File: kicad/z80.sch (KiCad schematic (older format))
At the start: 26 parts, among them J3 Conn_02x20_Odd_Even, J5 USB_B, J6 PWR, SW1 KS01Q, U1 Z80CPU, U2 74AHC14, U20 MIC5504-3.3YM5, U3 SST39SF010, U4 74AHC32, U5 AS6C1008-55PCN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

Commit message: Update to Kicad 5
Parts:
- C1, C2, C26, C3, C30, C4, C5, C6, C7: symbol C -> Device:C
- C24: symbol CP1_Small -> Device:CP1_Small
- D1: symbol LED_Small_ALT -> Device:LED_Small_ALT
- J3: symbol Conn_02x20_Odd_Even -> Connector_Generic:Conn_02x20_Odd_Even
- J5: symbol USB_B -> Connector:USB_B
- J6: symbol Conn_01x02 -> Connector_Generic:Conn_01x02
- R1, R18, R29: symbol R -> Device:R
- SW1: symbol SW_Push -> Switch:SW_Push
- U1: symbol Z80CPU -> CPU:Z80CPU
- U2: symbol 74HC14 -> 74xx:74HC14
- U20: symbol MIC5504-3.3YM5 -> Regulator_Linear:MIC5504-3.3YM5
- U3: symbol SST39SF010 -> Memory_Flash:SST39SF010
- U4: symbol 74LS32 -> 74xx:74LS32
- U5: symbol AS6C1008-55SIN -> headquarters:AS6C1008-55SIN
- U6: symbol 74LS138 -> 74xx:74LS138
- X1: symbol CXO_DIP8 -> Oscillator:CXO_DIP8
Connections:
- wire segments 237 -> 264

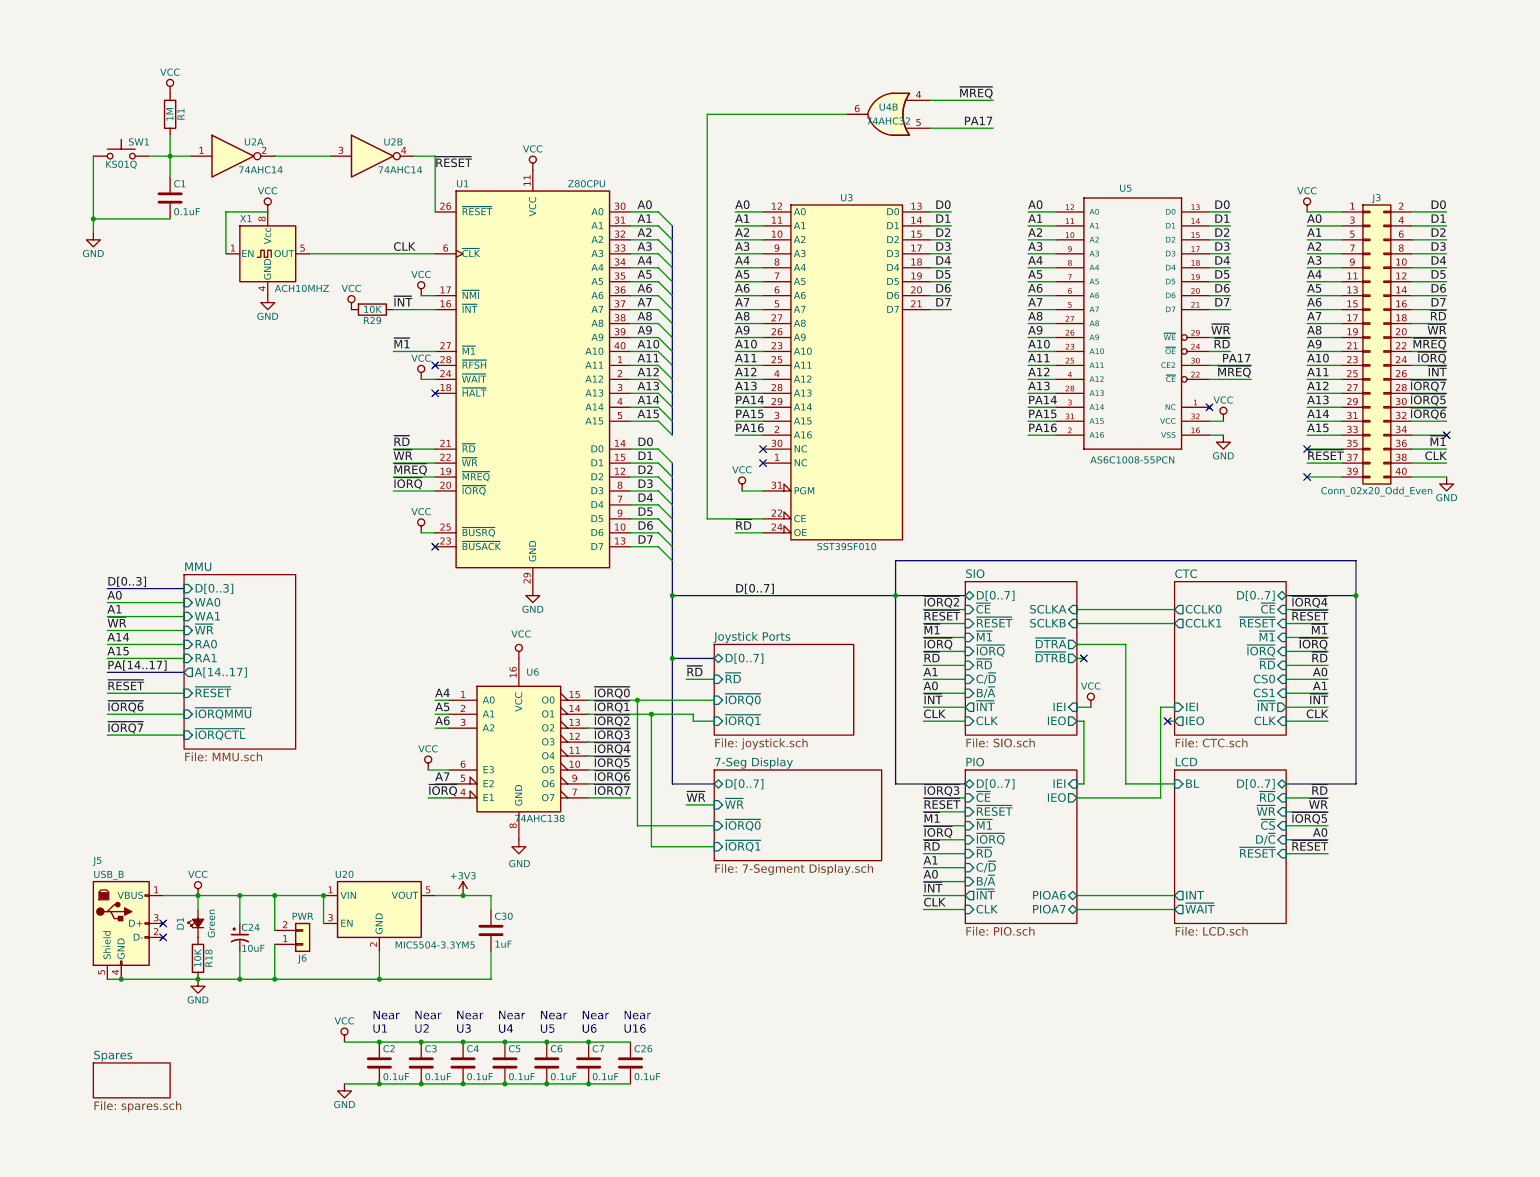
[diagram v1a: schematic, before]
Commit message: Working on SD card interface, cleaning up.
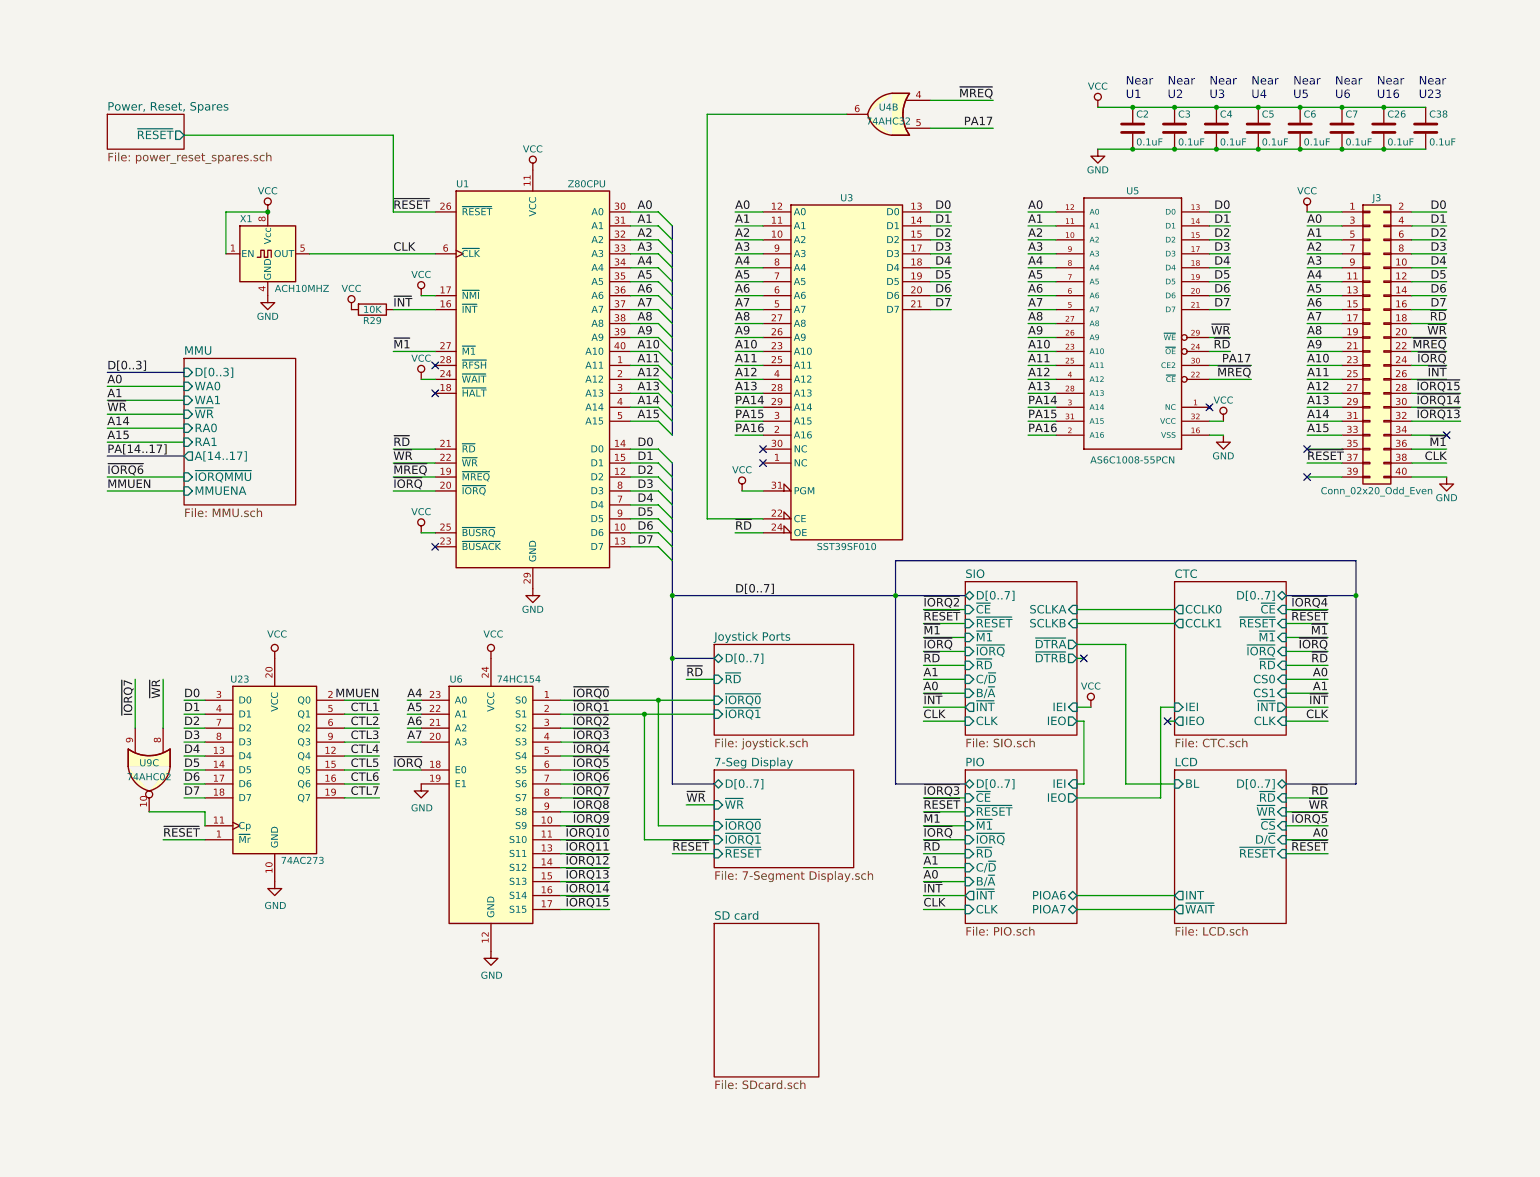
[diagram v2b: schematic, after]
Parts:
- removed C1: 0.1uF, Capacitors_THT:C_Disc_D4.3mm_W1.9mm_P5.00mm, symbol Device:C
- removed C24: 10uF, Capacitors_THT:CP_Radial_D5.0mm_P2.50mm, symbol Device:CP1_Small
- removed C30: 1uF, symbol Device:C
- removed D1: Green, LEDs:LED_D5.0mm, symbol Device:LED_Small_ALT
- removed J5: USB_B, z80_footprints:USB_B_E8144-B02022-L, symbol Connector:USB_B
- removed J6: PWR, Pin_Headers:Pin_Header_Straight_2x01_Pitch2.54mm, symbol Connector_Generic:Conn_01x02
- removed R1: 1M, Resistors_THT:R_Axial_DIN0204_L3.6mm_D1.6mm_P5.08mm_Horizontal, symbol Device:R
- removed R18: 10K, Resistors_THT:R_Axial_DIN0204_L3.6mm_D1.6mm_P5.08mm_Horizontal, symbol Device:R
- removed SW1: KS01Q, z80_footprints:KS-01Q-02, symbol Switch:SW_Push
- removed U2: 74AHC14, Housings_DIP:DIP-14_W7.62mm_LongPads, symbol 74xx:74HC14
- removed U20: MIC5504-3.3YM5, TO_SOT_Packages_SMD:SOT-23-5, symbol Regulator_Linear:MIC5504-3.3YM5
- removed U6: 74AHC138, Housings_DIP:DIP-16_W7.62mm_LongPads, symbol 74xx:74LS138
- added C38: 0.1uF, Capacitors_THT:C_Disc_D4.3mm_W1.9mm_P5.00mm, symbol Device:C
- added U23: 74AC273, symbol 74xx:74LS273
- added U6: 74HC154, symbol 74xx:74LS154
- added U9: 74AHC02, Housings_DIP:DIP-14_W7.62mm_LongPads, symbol 74xx:74HC02
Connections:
- net A4: now also U6.23 (A0)
- net A5: now also U6.22 (A1)
- net A6: now also U6.21 (A2)
- net A7: now also U6.20 (A3)
- net D0: now also U23.3 (D0)
- net D1: now also U23.4 (D1)
- net D2: now also U23.7 (D2)
- net D3: now also U23.8 (D3)
- net D4: now also U23.13 (D4)
- net D5: now also U23.14 (D5)
- net D6: now also U23.17 (D6)
- net D7: now also U23.18 (D7)
- net GND: now also C38.2, U23.10 (GND), U6.12 (GND), U6.19 (E1)
- net VCC: now also C38.1, U23.20 (VCC), U6.24 (VCC)
- net ~IORQ: now also U6.18 (E0)
- net ~IORQ0: now also U6.1 (S0)
- net ~IORQ1: now also U6.2 (S1)
- net ~IORQ2: now also U6.3 (S2)
- net ~IORQ3: now also U6.4 (S3)
- net ~IORQ4: now also U6.5 (S4)
- net ~IORQ5: now also U6.6 (S5); no longer J3.30 (Pin_30)
- net ~IORQ6: now also U6.7 (S6); no longer J3.32 (Pin_32)
- net ~IORQ7: now also U6.8 (S7), U9.9; no longer J3.28 (Pin_28)
- net ~RESET: now also U23.1 (~Mr)
- net ~WR: now also U9.8
- new net: U23.11 (Cp), U9.10
- new net CTL1: U23.5 (Q1)
- new net CTL2: U23.6 (Q2)
- new net CTL3: U23.9 (Q3)
- new net CTL4: U23.12 (Q4)
- new net CTL5: U23.15 (Q5)
- new net CTL6: U23.16 (Q6)
- new net CTL7: U23.19 (Q7)
- new net MMUEN: U23.2 (Q0)
- new net ~IORQ10: U6.11 (S10)
- new net ~IORQ11: U6.13 (S11)
- new net ~IORQ12: U6.14 (S12)
- new net ~IORQ13: J3.32 (Pin_32), U6.15 (S13)
- new net ~IORQ14: J3.30 (Pin_30), U6.16 (S14)
- new net ~IORQ15: J3.28 (Pin_28), U6.17 (S15)
- new net ~IORQ8: U6.9 (S8)
- new net ~IORQ9: U6.10 (S9)
- no-connect marks 13 -> 11
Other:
- note added: "Near\nU23"
- moved on the sheet: C2, C26, C3, C4, C5, C6, C7
